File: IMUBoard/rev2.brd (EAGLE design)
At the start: 49 x 43 mm, 25 parts, among them U1 SAM-M8Q, U2 V_REG_317SMD, U3 MAX3232, U4 OPENIMU

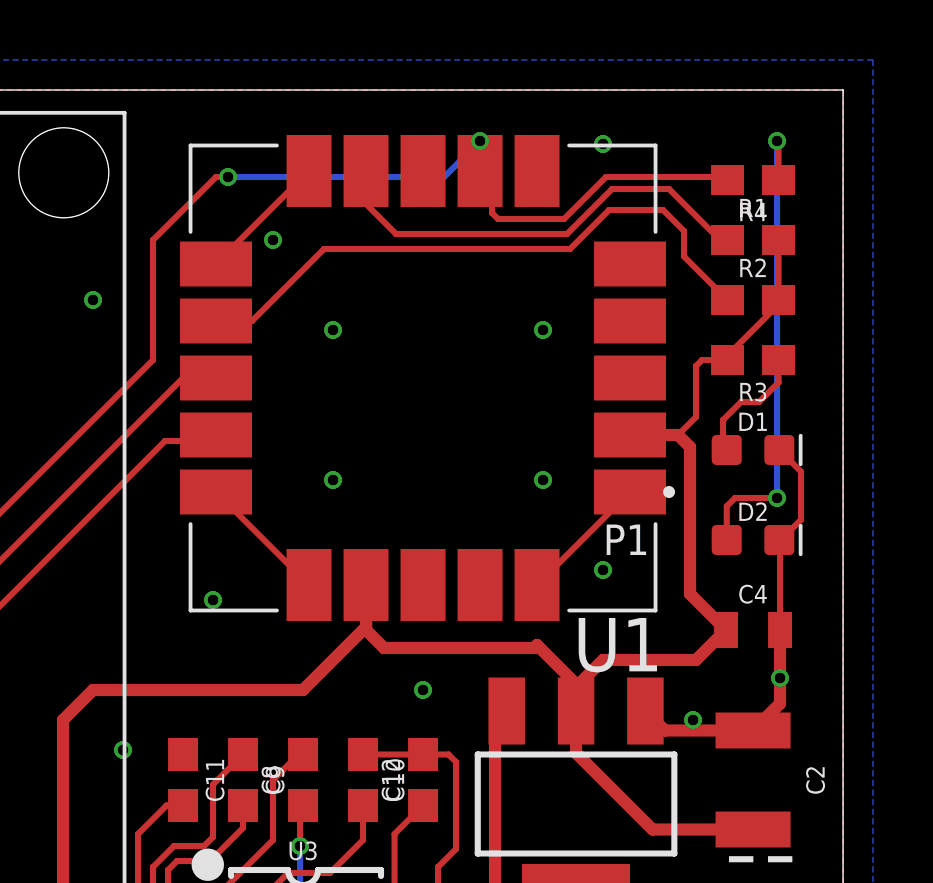
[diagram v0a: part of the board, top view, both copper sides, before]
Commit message: IMU board submit, doesn't work
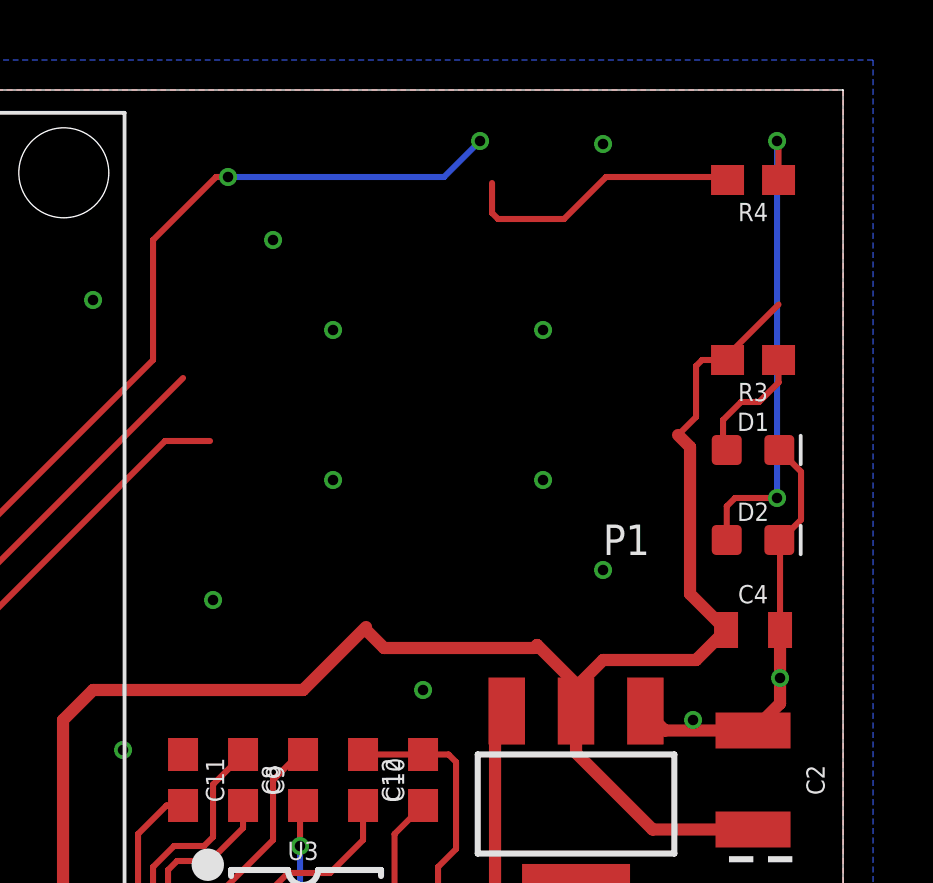
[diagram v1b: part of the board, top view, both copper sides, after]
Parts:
- removed R1, R2: 2.2k, SparkFun-Resistors:0603
- removed U1: SAM-M8Q, SAM-M8Q:XCVR_SAM-M8Q
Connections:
- removed net N$1: R1.1, U1.9
- removed net N$2: R2.1, U1.12
- removed net V_BCKP: U1.3
- net 3.3V: no longer R1.2, R2.2, U1.17, U1.2
- net GND: no longer U1.1, U1.10, U1.11, U1.15, U1.16, U1.20, U1.4, U1.5, U1.6
- net GPS_MISO: no longer U1.13
- net GPS_MOSI: no longer U1.14
- net PPS: no longer U1.7
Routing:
- net N$2: track 20.3 -> 0.00 mm
- net N$1: track 15.0 -> 0.00 mm
- net GND: track 49.8 -> 36.6 mm
- net 3.3V: track 85.9 -> 79.3 mm
- net PPS: track 63.6 -> 62.1 mm
- net GPS_MISO: track 40.0 -> 38.9 mm
